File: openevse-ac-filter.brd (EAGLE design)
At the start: 52.5 x 23 mm, 8 parts

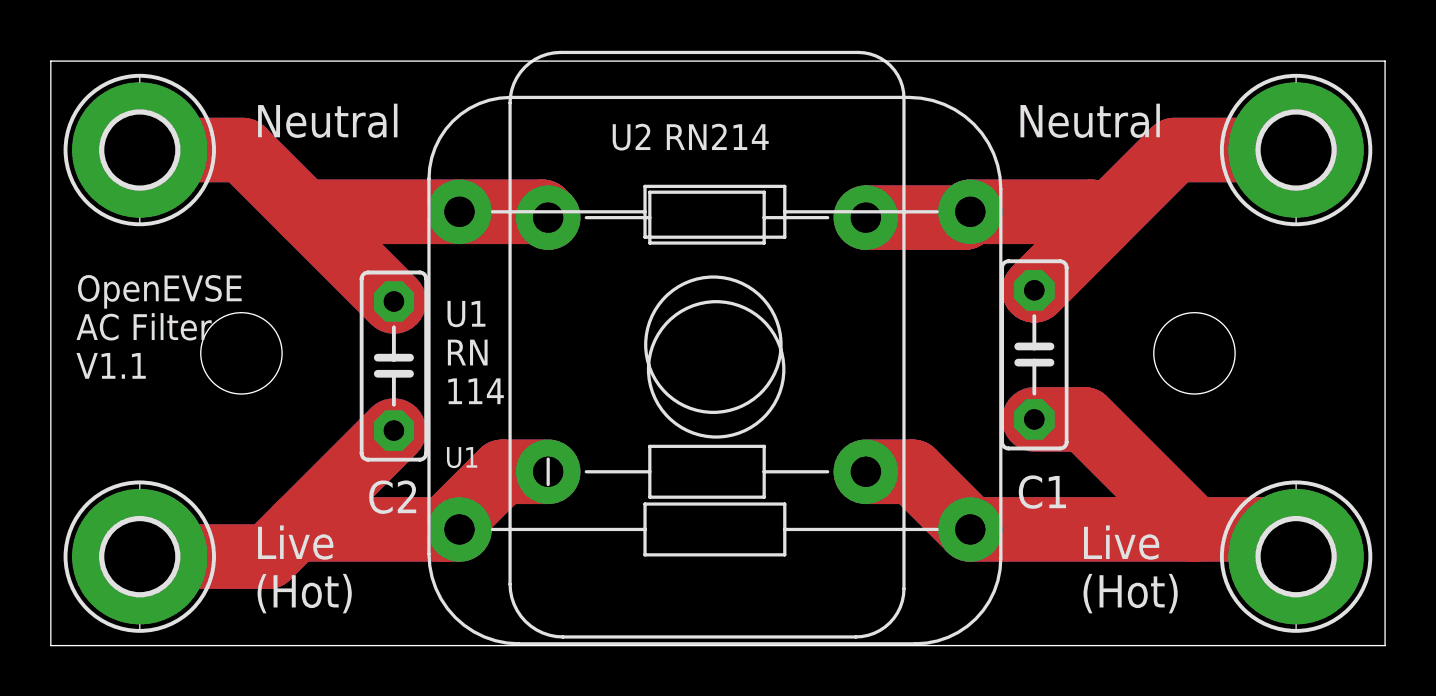
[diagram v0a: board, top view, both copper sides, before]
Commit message: V1.2 decrease hole size
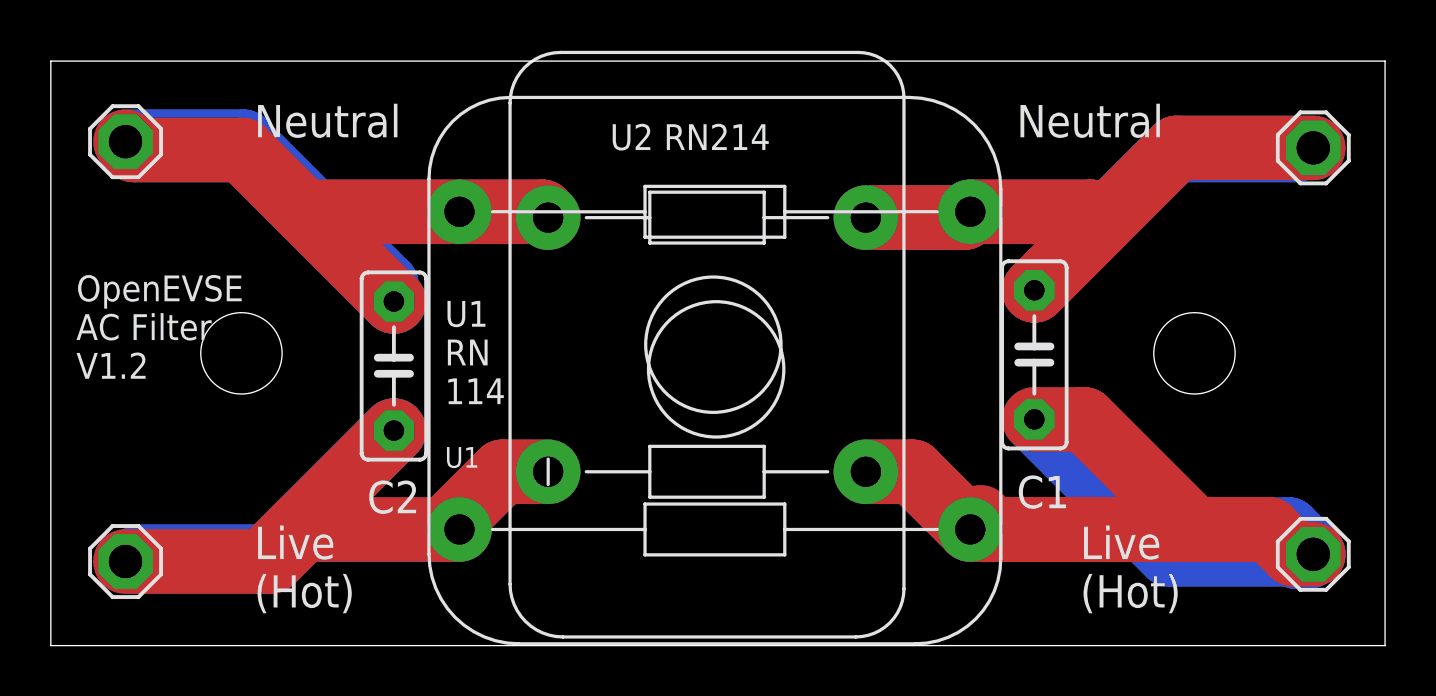
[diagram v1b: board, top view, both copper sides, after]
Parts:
- removed H2, H3, H4, H5: MOUNT-PAD-ROUND2.8, holes:2,8-PAD
- added LSP2, LSP3, LSP4, LSP5: SE13, solpad:SE13
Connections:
- net N$1: now also LSP2.MP; no longer H5.B2,8
- net N$2: now also LSP3.MP; no longer H2.B2,8
- net N$3: now also LSP5.MP; no longer H3.B2,8
- net N$4: now also LSP4.MP; no longer H4.B2,8
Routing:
- net N$1: track 26.9 -> 66.5 mm
- net N$5: track 26.9 -> 7.06 mm
- net N$3: track 23.4 -> 38.6 mm
- net N$4: track 22.2 -> 36.2 mm
- net N$2: track 25.9 -> 39.9 mm
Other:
- board text added: "OpenEVSE AC Filter V1.2"
- board text removed: "OpenEVSE AC Filter V1.1"
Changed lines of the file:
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@@
 <?xml version="1.0" encoding="utf-8"?>
 <!DOCTYPE eagle SYSTEM "eagle.dtd">
-<eagle version="7.7.0">
+<eagle version="8.3.1">
 <drawing>
 <settings>
 <setting alwaysvectorfont="no"/>
+<setting keepoldvectorfont="yes"/>
 <setting verticaltext="up"/>
 </settings>
-<grid distance="19.6850394" unitdist="mil" unit="mil" style="lines" multiple="1" display="yes" altdistance="0.025" altunitdist="inch" altunit="inch"/>
+<grid distance="20" unitdist="mil" unit="mil" style="lines" multiple="1" display="yes" altdistance="0.025" altunitdist="inch" altunit="inch"/>
 <layers>
-<layer number="1" name="Top" color="4" fill="1" visible="no" active="yes"/>
+<layer number="1" name="Top" color="4" fill="1" visible="yes" active="yes"/>
 <layer number="16" name="Bottom" color="1" fill="1" visible="yes" active="yes"/>
 <layer number="17" name="Pads" color="2" fill="1" visible="yes" active="yes"/>
@@
 <text x="1" y="8.5" size="1.016" layer="21" font="vector" ratio="18">OpenEVSE
 AC Filter
-V1.1
+V1.2
 </text>
 <text x="8" y="-0.5" size="1.27" layer="21" font="vector" ratio="18">Live
@@
 <attribute name="VALUE" x="11.794" y="6.968" size="1.27" layer="27" font="vector" ratio="18" rot="R90"/>
 </element>
-<element name="H2" library="holes" package="2,8-PAD" value="MOUNT-PAD-ROUND2.8" x="49" y="17.5"/>
-<element name="H3" library="holes" package="2,8-PAD" value="MOUNT-PAD-ROUND2.8" x="3.5" y="1.5"/>
-<element name="H4" library="holes" package="2,8-PAD" value="MOUNT-PAD-ROUND2.8" x="3.5" y="17.5"/>
-<element name="H5" library="holes" package="2,8-PAD" value="MOUNT-PAD-ROUND2.8" x="49" y="1.5"/>
+<element name="LSP2" library="solpad" library_urn="urn:adsk.eagle:library:364" package="SE13" package3d_urn="urn:adsk.eagle:package:26505/1" value="SE13" x="49.676" y="1.592" smashed="yes">
+<attribute name="VALUE" x="49.676" y="1.973" size="0.0254" layer="27"/>
+</element>
+<element name="LSP3" library="solpad" library_urn="urn:adsk.eagle:library:364" package="SE13" package3d_urn="urn:adsk.eagle:package:26505/1" value="SE13" x="49.676" y="17.584" smashed="yes">
+<attribute name="VALUE" x="49.676" y="17.965" size="0.0254" layer="27"/>
+</element>
+<element name="LSP4" library="solpad" library_urn="urn:adsk.eagle:library:364" package="SE13" package3d_urn="urn:adsk.eagle:package:26505/1" value="SE13" x="2.94" y="17.828" smashed="yes">
+<attribute name="VALUE" x="2.94" y="18.209" size="0.0254" layer="27"/>
+</element>
+<element name="LSP5" library="solpad" library_urn="urn:adsk.eagle:library:364" package="SE13" package3d_urn="urn:adsk.eagle:package:26505/1" value="SE13" x="2.94" y="1.308" smashed="yes">
+<attribute name="VALUE" x="2.94" y="1.689" size="0.0254" layer="27"/>
+</element>
 </elements>
 <signals>
@@
 <contactref element="U$2" pad="P$4"/>
 <contactref element="C1" pad="1"/>
-<contactref element="H5" pad="B2,8"/>
-<wire x1="49.5" y1="1.5" x2="49" y2="1.5" width="2.54" layer="1"/>
 <wire x1="32.07" y1="4.84" x2="33.91" y2="4.84" width="2.54" layer="1"/>
-<wire x1="33.91" y1="4.84" x2="36.18" y2="2.57" width="2.54" layer="1"/>
+<wire x1="36.18" y1="2.57" x2="33.91" y2="4.84" width="2.54" layer="1"/>
 <wire x1="36.18" y1="2.57" x2="45" y2="2.57" width="2.54" layer="1"/>
 <wire x1="45" y1="2.57" x2="47.93" y2="2.57" width="2.54" layer="1"/>
-<wire x1="47.93" y1="2.57" x2="49" y2="1.5" width="2.54" layer="1"/>
+<wire x1="40.67" y1="6.9" x2="45" y2="2.57" width="2.54" layer="1"/>
+<contactref element="LSP2" pad="MP"/>
+<wire x1="49.676" y1="1.592" x2="44.008" y2="1.592" width="2.54" layer="16"/>
+<wire x1="38.7" y1="6.9" x2="44.008" y2="1.592" width="2.54" layer="16"/>
+<wire x1="49.676" y1="1.592" x2="48.908" y2="1.592" width="2.54" layer="1"/>
+<wire x1="48.908" y1="1.592" x2="47.93" y2="2.57" width="2.54" layer="1"/>
+<wire x1="47.93" y1="2.57" x2="36.18" y2="2.57" width="2.54" layer="1"/>
 <wire x1="38.7" y1="6.9" x2="40.67" y2="6.9" width="2.54" layer="1"/>
-<wire x1="40.67" y1="6.9" x2="45" y2="2.57" width="2.54" layer="1"/>
+<wire x1="36.18" y1="2.57" x2="36.18" y2="2.652" width="2.54" layer="1"/>
+<wire x1="36.18" y1="2.652" x2="36.576" y2="3.048" width="2.54" layer="1"/>
+<wire x1="36.18" y1="2.57" x2="48.698" y2="2.57" width="2.54" layer="16"/>
+<wire x1="48.698" y1="2.57" x2="49.676" y2="1.592" width="2.54" layer="16"/>
 </signal>
 <signal name="N$2">
@@
 <wire x1="32.07" y1="14.84" x2="35.95" y2="14.84" width="2.54" layer="1"/>
 <wire x1="35.95" y1="14.84" x2="36.18" y2="15.07" width="2.54" layer="1"/>
-<wire x1="45.72" y1="19" x2="41.36" y2="14.64" width="0" layer="19" extent="1-16"/>
-<wire x1="41.36" y1="14.64" x2="38.7" y2="11.98" width="2.54" layer="1"/>
+<wire x1="38.7" y1="11.98" x2="41.36" y2="14.64" width="2.54" layer="1"/>
 <wire x1="36.18" y1="15.07" x2="40.93" y2="15.07" width="2.54" layer="1"/>
 <wire x1="40.93" y1="15.07" x2="41.36" y2="14.64" width="2.54" layer="1"/>
-<contactref element="H2" pad="B2,8"/>
-<wire x1="49" y1="17.5" x2="44.22" y2="17.5" width="2.54" layer="1"/>
-<wire x1="44.22" y1="17.5" x2="38.7" y2="11.98" width="2.54" layer="1"/>
+<contactref element="LSP3" pad="MP"/>
+<wire x1="49.676" y1="17.584" x2="44.304" y2="17.584" width="2.54" layer="16"/>
+<wire x1="44.304" y1="17.584" x2="38.7" y2="11.98" width="2.54" layer="16"/>
+<wire x1="49.676" y1="17.584" x2="44.304" y2="17.584" width="2.54" layer="1"/>
+<wire x1="44.304" y1="17.584" x2="38.7" y2="11.98" width="2.54" layer="1"/>
 </signal>
 <signal name="N$3">
@@
 <wire x1="9.77" y1="2.73" x2="13.5" y2="6.46" width="2.54" layer="1"/>
 <wire x1="16.08" y1="2.57" x2="15.5" y2="2.57" width="2.54" layer="1"/>
-<wire x1="15.5" y1="2.57" x2="9.93" y2="2.57" width="2.54" layer="1"/>
+<wire x1="9.93" y1="2.57" x2="15.5" y2="2.57" width="2.54" layer="1"/>
 <wire x1="9.93" y1="2.57" x2="9.77" y2="2.73" width="2.54" layer="1"/>
 <wire x1="19.57" y1="4.84" x2="17.77" y2="4.84" width="2.54" layer="1"/>
 <wire x1="17.77" y1="4.84" x2="15.5" y2="2.57" width="2.54" layer="1"/>
-<contactref element="H3" pad="B2,8"/>
-<wire x1="3.5" y1="1.5" x2="8.54" y2="1.5" width="2.54" layer="1"/>
 <wire x1="8.54" y1="1.5" x2="9.77" y2="2.73" width="2.54" layer="1"/>
+<contactref element="LSP5" pad="MP"/>
+<wire x1="2.94" y1="1.308" x2="8.348" y2="1.308" width="2.54" layer="16"/>
+<wire x1="8.348" y1="1.308" x2="13.5" y2="6.46" width="2.54" layer="16"/>
+<wire x1="2.94" y1="1.308" x2="8.668" y2="1.308" width="2.54" layer="1"/>
+<wire x1="8.668" y1="1.308" x2="9.93" y2="2.57" width="2.54" layer="1"/>
 </signal>
 <signal name="N$4">
@@
 <wire x1="16.08" y1="15.07" x2="19.34" y2="15.07" width="2.54" layer="1"/>
 <wire x1="19.34" y1="15.07" x2="19.57" y2="14.84" width="2.54" layer="1"/>
-<contactref element="H4" pad="B2,8"/>
-<wire x1="3.5" y1="17.5" x2="7.54" y2="17.5" width="2.54" layer="1"/>
-<wire x1="7.54" y1="17.5" x2="9.97" y2="15.07" width="2.54" layer="1"/>
+<wire x1="9.97" y1="15.07" x2="7.54" y2="17.5" width="2.54" layer="1"/>
+<contactref element="LSP4" pad="MP"/>
+<wire x1="2.94" y1="17.828" x2="7.572" y2="17.828" width="2.54" layer="16"/>
+<wire x1="7.572" y1="17.828" x2="13.208" y2="12.192" width="2.54" layer="16"/>
+<wire x1="13.208" y1="12.192" x2="13.208" y2="11.832" width="2.54" layer="16"/>
+<wire x1="13.208" y1="11.832" x2="13.5" y2="11.54" width="2.54" layer="16"/>
+<wire x1="7.54" y1="17.5" x2="3.268" y2="17.5" width="2.54" layer="1"/>
+<wire x1="3.268" y1="17.5" x2="2.94" y2="17.828" width="2.54" layer="1"/>
+</signal>
+<signal name="N$9">
+<wire x1="38.7" y1="6.9" x2="40.67" y2="6.9" width="0" layer="19" extent="1-16"/>
 </signal>
 <signal name="N$5">
@@
 <wire x1="32.07" y1="4.84" x2="33.91" y2="4.84" width="2.54" layer="16"/>
 <wire x1="33.91" y1="4.84" x2="36.18" y2="2.57" width="2.54" layer="16"/>
-<wire x1="36.18" y1="2.57" x2="45" y2="2.57" width="2.54" layer="16"/>
-<wire x1="45" y1="2.57" x2="47.93" y2="2.57" width="2.54" layer="16"/>
+<wire x1="36.18" y1="2.57" x2="47.93" y2="2.57" width="0" layer="19" extent="1-16"/>
 <wire x1="47.93" y1="2.57" x2="49" y2="1.5" width="2.54" layer="16"/>
-<wire x1="38.7" y1="6.9" x2="40.67" y2="6.9" width="2.54" layer="16"/>
-<wire x1="40.67" y1="6.9" x2="45" y2="2.57" width="2.54" layer="16"/>
 </signal>
 <signal name="N$6">
@@
 which will not be processed correctly with this version.
 </note>
+<note version="8.2" severity="warning">
+Since Version 8.2, EAGLE supports online libraries. The ids
+of those online libraries will not be understood (or retained)
+with this version.
+</note>
+<note version="8.3" severity="warning">
+Since Version 8.3, EAGLE supports URNs for individual library
+assets (packages, symbols, and devices). The URNs of those assets
+will not be understood (or retained) with this version.
+</note>
+<note version="8.3" severity="warning">
+Since Version 8.3, EAGLE supports the association of 3D packages
+with devices in libraries, schematics, and board files. Those 3D
+packages will not be understood (or retained) with this version.
+</note>
 </compatibility>

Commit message: smaller dimensions
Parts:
- moved LSP2 1.02 mm to (48.7, 1.59)
- moved LSP3 1.02 mm to (48.7, 17.6)
- moved LSP4 1.02 mm to (3.96, 17.8)
- moved LSP5 1.02 mm to (3.96, 1.31)
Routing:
- net N$1: track 66.5 -> 52.8 mm
- net N$2: track 39.9 -> 37.9 mm
- net N$3: track 38.6 -> 36.6 mm
- net N$4: track 36.2 -> 35.5 mm
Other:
- board size 52.5 x 23 mm -> 48.4 x 23 mm
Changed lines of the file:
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@@
 <grid distance="20" unitdist="mil" unit="mil" style="lines" multiple="1" display="yes" altdistance="0.025" altunitdist="inch" altunit="inch"/>
 <layers>
-<layer number="1" name="Top" color="4" fill="1" visible="yes" active="yes"/>
-<layer number="16" name="Bottom" color="1" fill="1" visible="yes" active="yes"/>
+<layer number="1" name="Top" color="4" fill="1" visible="no" active="yes"/>
+<layer number="16" name="Bottom" color="1" fill="1" visible="no" active="yes"/>
 <layer number="17" name="Pads" color="2" fill="1" visible="yes" active="yes"/>
 <layer number="18" name="Vias" color="2" fill="1" visible="yes" active="yes"/>
@@
 <board>
 <plain>
-<wire x1="0" y1="-2" x2="52.5" y2="-2" width="0" layer="20"/>
-<wire x1="52.5" y1="-2" x2="52.5" y2="21" width="0" layer="20"/>
-<wire x1="52.5" y1="21" x2="0" y2="21" width="0" layer="20"/>
-<wire x1="0" y1="21" x2="0" y2="-2" width="0" layer="20"/>
+<wire x1="2.032" y1="-2" x2="50.468" y2="-2" width="0" layer="20"/>
+<wire x1="50.468" y1="-2" x2="50.468" y2="21" width="0" layer="20"/>
+<wire x1="50.468" y1="21" x2="2.032" y2="21" width="0" layer="20"/>
+<wire x1="2.032" y1="21" x2="2.032" y2="-2" width="0" layer="20"/>
 <text x="22" y="17.5" size="1.016" layer="25" font="vector" ratio="18">U2 RN214</text>
 <text x="15.5" y="7.5" size="1.016" layer="25" font="vector" ratio="18">U1
@@
 <hole x="7.5" y="9.5" drill="3.2"/>
 <hole x="45" y="9.5" drill="3.2"/>
-<text x="1" y="8.5" size="1.016" layer="21" font="vector" ratio="18">OpenEVSE
+<text x="2.524" y="9.516" size="1.016" layer="21" font="vector" ratio="18">OpenEVSE
 AC Filter
 V1.2
@@
 <attribute name="VALUE" x="11.794" y="6.968" size="1.27" layer="27" font="vector" ratio="18" rot="R90"/>
 </element>
-<element name="LSP2" library="solpad" library_urn="urn:adsk.eagle:library:364" package="SE13" package3d_urn="urn:adsk.eagle:package:26505/1" value="SE13" x="49.676" y="1.592" smashed="yes">
-<attribute name="VALUE" x="49.676" y="1.973" size="0.0254" layer="27"/>
-</element>
-<element name="LSP3" library="solpad" library_urn="urn:adsk.eagle:library:364" package="SE13" package3d_urn="urn:adsk.eagle:package:26505/1" value="SE13" x="49.676" y="17.584" smashed="yes">
-<attribute name="VALUE" x="49.676" y="17.965" size="0.0254" layer="27"/>
-</element>
-<element name="LSP4" library="solpad" library_urn="urn:adsk.eagle:library:364" package="SE13" package3d_urn="urn:adsk.eagle:package:26505/1" value="SE13" x="2.94" y="17.828" smashed="yes">
-<attribute name="VALUE" x="2.94" y="18.209" size="0.0254" layer="27"/>
-</element>
-<element name="LSP5" library="solpad" library_urn="urn:adsk.eagle:library:364" package="SE13" package3d_urn="urn:adsk.eagle:package:26505/1" value="SE13" x="2.94" y="1.308" smashed="yes">
-<attribute name="VALUE" x="2.94" y="1.689" size="0.0254" layer="27"/>
+<element name="LSP2" library="solpad" library_urn="urn:adsk.eagle:library:364" package="SE13" package3d_urn="urn:adsk.eagle:package:26505/1" value="SE13" x="48.66" y="1.592" smashed="yes">
+<attribute name="VALUE" x="48.66" y="1.973" size="0.0254" layer="27"/>
+</element>
+<element name="LSP3" library="solpad" library_urn="urn:adsk.eagle:library:364" package="SE13" package3d_urn="urn:adsk.eagle:package:26505/1" value="SE13" x="48.66" y="17.584" smashed="yes">
+<attribute name="VALUE" x="48.66" y="17.965" size="0.0254" layer="27"/>
+</element>
+<element name="LSP4" library="solpad" library_urn="urn:adsk.eagle:library:364" package="SE13" package3d_urn="urn:adsk.eagle:package:26505/1" value="SE13" x="3.956" y="17.828" smashed="yes">
+<attribute name="VALUE" x="3.956" y="18.209" size="0.0254" layer="27"/>
+</element>
+<element name="LSP5" library="solpad" library_urn="urn:adsk.eagle:library:364" package="SE13" package3d_urn="urn:adsk.eagle:package:26505/1" value="SE13" x="3.956" y="1.308" smashed="yes">
+<attribute name="VALUE" x="3.956" y="1.689" size="0.0254" layer="27"/>
 </element>
 </elements>
@@
 <wire x1="32.07" y1="4.84" x2="33.91" y2="4.84" width="2.54" layer="1"/>
 <wire x1="36.18" y1="2.57" x2="33.91" y2="4.84" width="2.54" layer="1"/>
-<wire x1="36.18" y1="2.57" x2="45" y2="2.57" width="2.54" layer="1"/>
 <wire x1="45" y1="2.57" x2="47.93" y2="2.57" width="2.54" layer="1"/>
 <wire x1="40.67" y1="6.9" x2="45" y2="2.57" width="2.54" layer="1"/>
 <contactref element="LSP2" pad="MP"/>
-<wire x1="49.676" y1="1.592" x2="44.008" y2="1.592" width="2.54" layer="16"/>
+<wire x1="48.66" y1="1.592" x2="44.008" y2="1.592" width="2.54" layer="16"/>
 <wire x1="38.7" y1="6.9" x2="44.008" y2="1.592" width="2.54" layer="16"/>
-<wire x1="49.676" y1="1.592" x2="48.908" y2="1.592" width="2.54" layer="1"/>
+<wire x1="48.66" y1="1.592" x2="48.908" y2="1.592" width="2.54" layer="1"/>
 <wire x1="48.908" y1="1.592" x2="47.93" y2="2.57" width="2.54" layer="1"/>
-<wire x1="47.93" y1="2.57" x2="36.18" y2="2.57" width="2.54" layer="1"/>
+<wire x1="45" y1="2.57" x2="36.18" y2="2.57" width="2.54" layer="1"/>
 <wire x1="38.7" y1="6.9" x2="40.67" y2="6.9" width="2.54" layer="1"/>
 <wire x1="36.18" y1="2.57" x2="36.18" y2="2.652" width="2.54" layer="1"/>
 <wire x1="36.18" y1="2.652" x2="36.576" y2="3.048" width="2.54" layer="1"/>
 <wire x1="36.18" y1="2.57" x2="48.698" y2="2.57" width="2.54" layer="16"/>
-<wire x1="48.698" y1="2.57" x2="49.676" y2="1.592" width="2.54" layer="16"/>
+<wire x1="48.698" y1="2.57" x2="48.66" y2="1.592" width="2.54" layer="16"/>
 </signal>
 <signal name="N$2">
@@
 <wire x1="40.93" y1="15.07" x2="41.36" y2="14.64" width="2.54" layer="1"/>
 <contactref element="LSP3" pad="MP"/>
-<wire x1="49.676" y1="17.584" x2="44.304" y2="17.584" width="2.54" layer="16"/>
+<wire x1="48.66" y1="17.584" x2="44.304" y2="17.584" width="2.54" layer="16"/>
 <wire x1="44.304" y1="17.584" x2="38.7" y2="11.98" width="2.54" layer="16"/>
-<wire x1="49.676" y1="17.584" x2="44.304" y2="17.584" width="2.54" layer="1"/>
+<wire x1="48.66" y1="17.584" x2="44.304" y2="17.584" width="2.54" layer="1"/>
 <wire x1="44.304" y1="17.584" x2="38.7" y2="11.98" width="2.54" layer="1"/>
 </signal>
@@
 <wire x1="8.54" y1="1.5" x2="9.77" y2="2.73" width="2.54" layer="1"/>
 <contactref element="LSP5" pad="MP"/>
-<wire x1="2.94" y1="1.308" x2="8.348" y2="1.308" width="2.54" layer="16"/>
+<wire x1="3.956" y1="1.308" x2="8.348" y2="1.308" width="2.54" layer="16"/>
 <wire x1="8.348" y1="1.308" x2="13.5" y2="6.46" width="2.54" layer="16"/>
-<wire x1="2.94" y1="1.308" x2="8.668" y2="1.308" width="2.54" layer="1"/>
+<wire x1="3.956" y1="1.308" x2="8.668" y2="1.308" width="2.54" layer="1"/>
 <wire x1="8.668" y1="1.308" x2="9.93" y2="2.57" width="2.54" layer="1"/>
 </signal>
@@
 <wire x1="9.97" y1="15.07" x2="7.54" y2="17.5" width="2.54" layer="1"/>
 <contactref element="LSP4" pad="MP"/>
-<wire x1="2.94" y1="17.828" x2="7.572" y2="17.828" width="2.54" layer="16"/>
+<wire x1="3.956" y1="17.828" x2="7.572" y2="17.828" width="2.54" layer="16"/>
 <wire x1="7.572" y1="17.828" x2="13.208" y2="12.192" width="2.54" layer="16"/>
 <wire x1="13.208" y1="12.192" x2="13.208" y2="11.832" width="2.54" layer="16"/>
 <wire x1="13.208" y1="11.832" x2="13.5" y2="11.54" width="2.54" layer="16"/>
 <wire x1="7.54" y1="17.5" x2="3.268" y2="17.5" width="2.54" layer="1"/>
-<wire x1="3.268" y1="17.5" x2="2.94" y2="17.828" width="2.54" layer="1"/>
+<wire x1="3.268" y1="17.5" x2="3.956" y2="17.828" width="2.54" layer="1"/>
 </signal>
 <signal name="N$9">
